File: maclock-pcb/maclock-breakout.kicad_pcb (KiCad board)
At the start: 2 copper layers, 70.5 x 26.5 mm, 24 parts, among them J1 53398-0271, J2 53398-0471, J3 53398-0271, J4 Pi GPIO, SW1 TSB001A3518A, SW2 TSB001A3518A, U1 PAM8302AASCR, U2 SN74LVC1G17DBVR, U3 TPS7A2030PDBVR

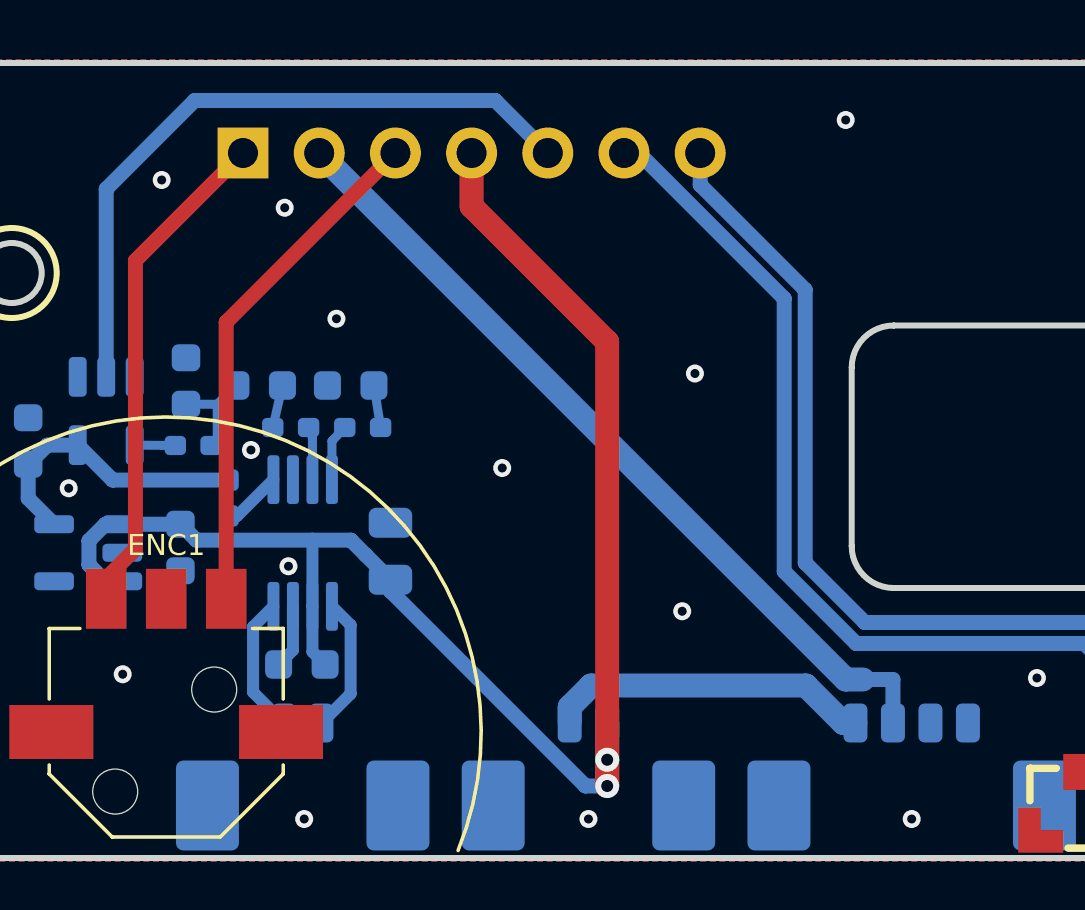
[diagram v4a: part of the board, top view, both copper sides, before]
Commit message: Breakout: spare C6 pads for a second amp input pole
R3/C1 is a single pole at 16 kHz, so it takes only about 24 dB off the
Pi's PWM noise near the PAM8302A's own 200-300 kHz switching frequency,
where a class-D amp can fold it back into the audio band. TI says as much
for DAC-fed class-D amps (TPA2011D1), and the Pi's own audio, which uses
the same buffer-on-LDO plus single RC as rev 2026.11, drives headphones,
not a switching amp.

C6 is a 470 pF C0G 0402 (Samsung CL05C471JB5NNNC, LCSC C307449) across
IN+ and IN-. With R4/R5 and the chip's internal 10 kOhm inputs it adds a
pole near 20 kHz: about 46 dB at 250 kHz instead of 24, for about 1 dB at
10 kHz. Rev 2026.10 had the same single pole and none of its measured
noise traced to this, so C6 is not fitted (DNP, off the BOM and the
placement file); solder it on only if a 2026.11 board hisses or whistles.

Layout: R5 and C6 stand vertically side by side east of R4, so C6's pads
sit on the IN+ run from R4 and the IN- run to U1 pin 4. C2, C3 and R4
stay below the Dial A / Dial B labels. NT1 turns vertical with its GND
pad on J2 pin 3, so the Pi's ground still joins the board ground at the
power connector. The schematic shows C6 as a small capacitor across the
IN+/IN- wires.

ERC 0. DRC 0 errors, 0 unconnected, schematic parity clean; only the
existing title-text thickness warning.
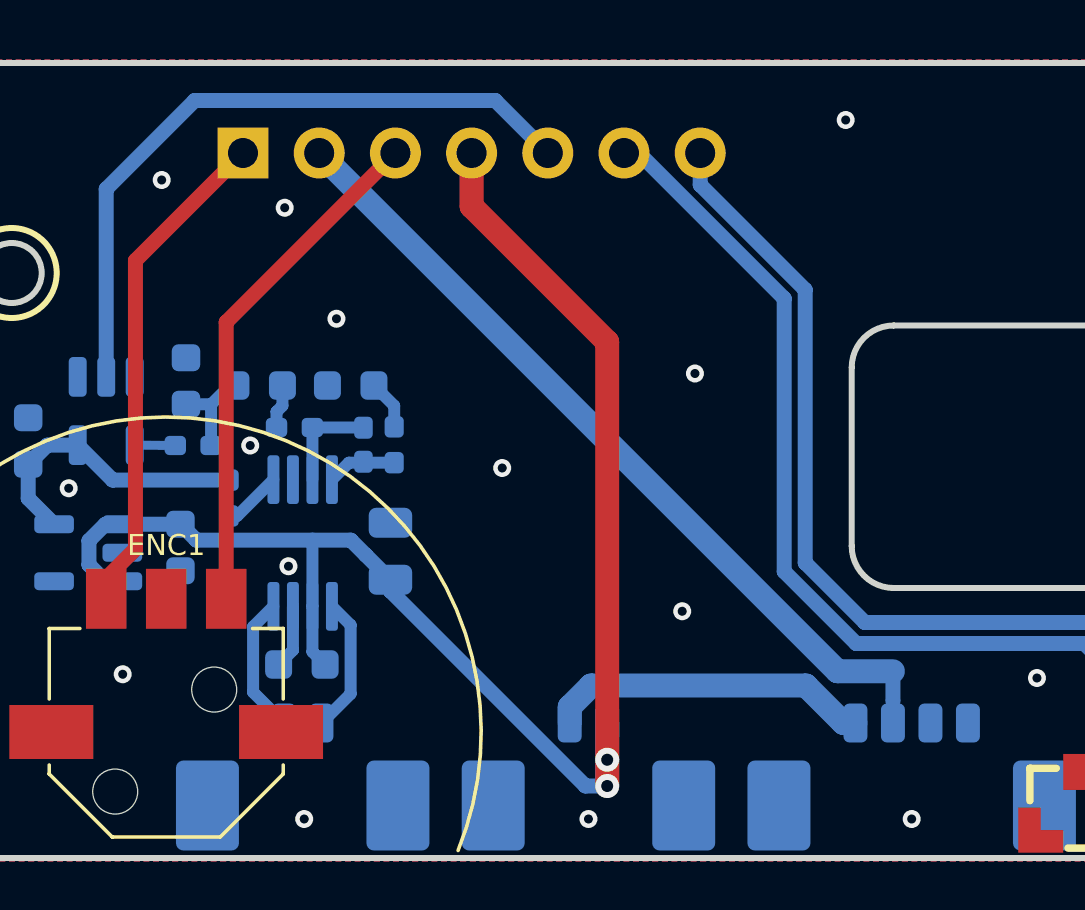
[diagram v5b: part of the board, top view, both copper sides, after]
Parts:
- added C6: 470pF, Capacitor_SMD:C_0402_1005Metric_Pad0.74x0.62mm_HandSolder, B.Cu at (133.5, 90.7)
- moved R5 1.20 mm to (134.5, 90.7), turned to -90 degrees
- moved NT1 0.55 mm to (151.1, 98.8), turned to -90 degrees
- moved R4 0.12 mm to (131.2, 90.2)
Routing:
- net Net-(U1-IN+): track 1.76 -> 3.44 mm
- net GND: track 3.59 -> 2.14 mm
- net /GND_PI: track 25.4 -> 26.3 mm

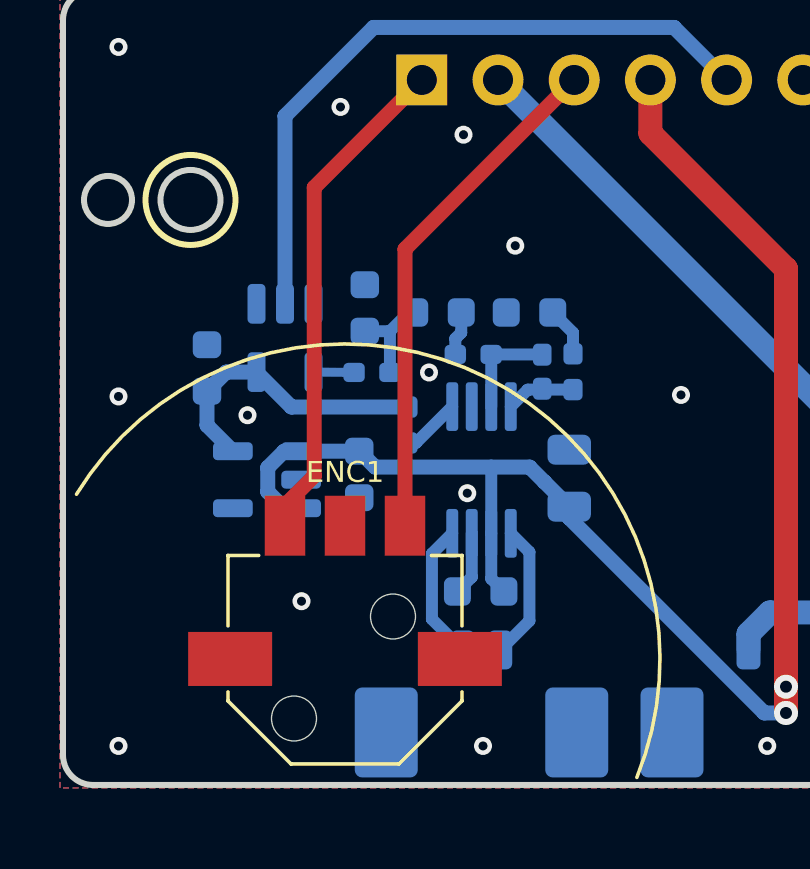
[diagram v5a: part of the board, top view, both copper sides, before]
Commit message: Breakout: ENC1 is a HUANO 4.5 laid flat, pins north, fitted by hand
No vertical encoder at LCSC, DigiKey or Mouser grips the dial: the bores
are too loose or too short. A HUANO 4.5 mm mouse-wheel encoder laid on its
back does: its 1.74 mm bore and 5 mm-thick body reach the full-width part of
the dial's tapered shaft. Nothing like it is sold where PCBway buys, so ENC1
is fitted by hand.

- maclock:RotaryEncoder_HUANO_4.5mm_LayFlat_SMD, origin on the bore at the
  old ENC1 spot, pins pointing north. Top-side pads at 2.5 mm pitch for the
  pins, bent down, plus two MP pads for the frame's clip legs. HUANO
  publishes no drawing, so the pads run 2.8 mm north from just outside the
  body (estimated from the listing photo) to catch the pins wherever they
  land. No paste, thermal reliefs on the GND pads, no 3D model. E8E8
  footprint and model removed.
- Pin order assumed C-B-A with the common at one end, as on HOAUC's and
  TT's mouse-wheel encoders: C (west pad) = GND, B = ENC_B, A = ENC_A.
  Turning the part face-down swaps the two ends.
- ENC_A and ENC_B re-routed on F.Cu to the new pads; nothing else moves.
- ENC1 is out of the BOM and placement files (not DNP: it is fitted, just
  not by PCBway). Symbol renamed maclock:RotaryEncoder_HUANO_4.5mm, with
  Amazon as the supplier; the schematic note and README say how to fit it.

DRC as before (one text-thickness warning), 0 unconnected, schematic parity
clean, ERC 0.
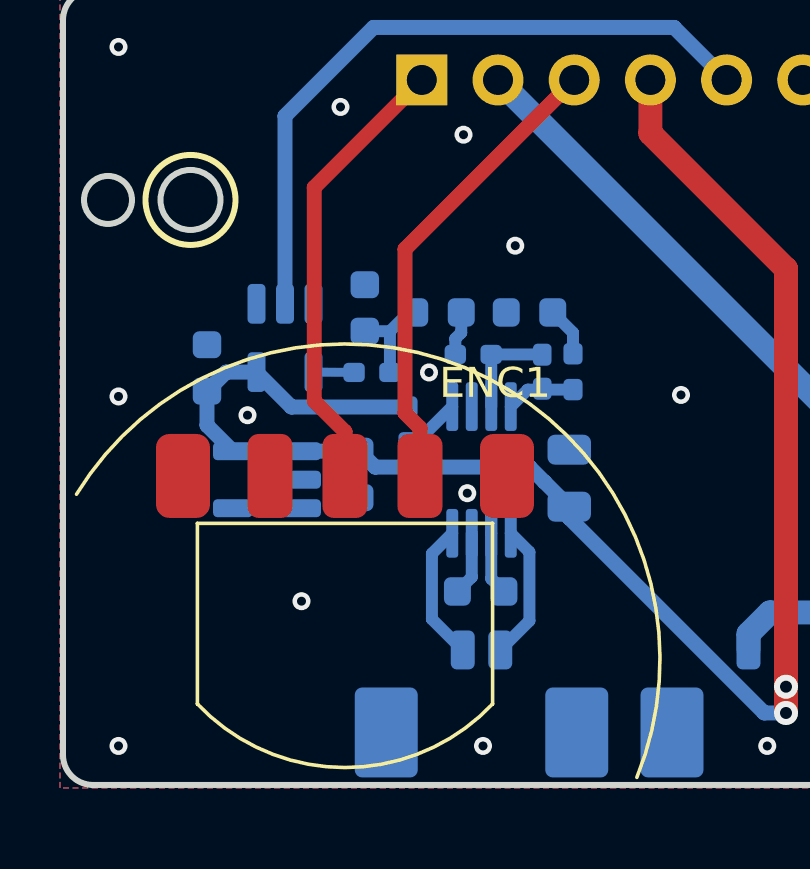
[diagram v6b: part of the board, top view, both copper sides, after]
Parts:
- ENC1: value E8E8-3.2C60-9B34 -> HUANO 4.5; footprint maclock:RotaryEncoder_E8E8-3.2C60-9B34_SMD -> maclock:RotaryEncoder_HUANO_4.5mm_LayFlat_SMD
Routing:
- net /ENC_B: track 16.7 -> 15.1 mm
- net /ENC_A: track 17.2 -> 15.7 mm
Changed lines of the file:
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@@
 		)
 	)
-	(footprint "maclock:RotaryEncoder_E8E8-3.2C60-9B34_SMD"
+	(footprint "maclock:RotaryEncoder_HUANO_4.5mm_LayFlat_SMD"
 		(layer "F.Cu")
 		(at 126.9 100.3)
-		(descr "F-Switch E8E8-3.2C60-9B34 SMD mouse-wheel encoder, 7.8 x 6.95 x 3.2 mm, 1.74 mm hex bore perpendicular to the board, 9 pulse / 18 detent (dicomon item 1037). Origin = bore centre. Copper is the proto board Dial land the encoder was soldered to; body outline measured from a real part. Silk carries the body outline and the 21 mm wheel circle, clipped to the maclock-breakout board edge.")
-		(tags "encoder wheel mouse F-Switch E8E8 hex bore")
+		(descr "HUANO 4.5 mm mouse-wheel encoder (sold as MECCANIXITY, Amazon B0C13ZZVT5) laid on its back with the 1.74 mm hex bore up, pins pointing north and bent down onto top-side pads; the MP pads take the frame's two clip legs, bent down the same way. Origin = bore centre. HUANO publishes no drawing: the 9.6 mm width and 2.5 mm pin pitch are the listing's, and the bore sits about 4.4 mm from the pin edge and 3.5 mm from the domed end (estimated from the listing photo), so the pads run 2.8 mm north to catch the bent pins wherever they land. Pin order assumed C-B-A with the common at one end, as on HOAUC's and TT's mouse-wheel encoders; turning the part face-down swaps the two ends. Hand-fitted, so no paste.")
+		(tags "encoder wheel mouse HUANO 4.5 hex bore lay flat")
 		(property "Reference" "ENC1"
-			(at 0 -6.225 0)
+			(at 5 -9.2 0)
 			(layer "F.SilkS")
 			(effects
 				(font
-					(size 0.7 0.7)
+					(size 1 1)
 					(thickness 0.15)
 				)
 			)
 		)
-		(property "Value" "E8E8-3.2C60-9B34"
-			(at 0 4.6 0)
+		(property "Value" "HUANO 4.5"
+			(at 0 2.4 0)
 			(layer "F.Fab")
 			(effects
@@
 			)
 		)
-		(property "Datasheet" "https://www.dicomon.com/index.php?ctl=Product&met=detail&item_id=1037"
+		(property "Datasheet" ""
 			(at 0 0 0)
 			(layer "F.Fab")
@@
 			)
 		)
-		(property "Description" "F-Switch E8E8-3.2C60-9B34 SMD mouse-wheel encoder, 9 pulse / 18 detent, 1.74 mm hex bore; MP = the cover's solder tabs"
+		(property "Description" "HUANO 4.5 mm mouse-wheel encoder laid on its back, 1.74 mm hex bore up, legs bent down onto top-side pads; MP = the frame's clip legs. Hand-fitted"
 			(at 0 0 0)
 			(layer "F.Fab")
@@
 			)
 		)
-		(property "Manufacturer" "F-Switch"
+		(property "Manufacturer" "HUANO"
 			(at 0 0 0)
 			(layer "F.Fab")
@@
 			)
 		)
-		(property "MPN" "E8E8-3.2C60-9B34"
+		(property "MPN" ""
 			(at 0 0 0)
 			(layer "F.Fab")
@@
 			)
 		)
-		(property "Supplier" "dicomon"
+		(property "Supplier" "Amazon"
 			(at 0 0 0)
 			(layer "F.Fab")
@@
 			)
 		)
-		(property "Supplier Link" "https://www.dicomon.com/index.php?ctl=Product&met=detail&item_id=1037"
+		(property "Supplier Link" "https://www.amazon.com/dp/B0C13ZZVT5"
 			(at 0 0 0)
 			(layer "F.Fab")
@@
 			)
 		)
-		(attr smd)
+		(zone_connect 1)
+		(attr smd exclude_from_pos_files exclude_from_bom)
 		(duplicate_pad_numbers_are_jumpers no)
 		(fp_line
-			(start -3.9 -3.45)
-			(end -3.9 -1.1)
+			(start -4.92 -4.52)
+			(end 4.92 -4.52)
 			(stroke
 				(width 0.12)
@@
 		)
 		(fp_line
-			(start -3.9 -3.45)
-			(end -2.875 -3.45)
+			(start -4.92 1.5)
+			(end -4.92 -4.52)
 			(stroke
 				(width 0.12)
@@
 		)
 		(fp_line
-			(start -3.9 1.1)
-			(end -3.9 1.4)
+			(start 4.92 -4.52)
+			(end 4.92 1.5)
 			(stroke
 				(width 0.12)
@@
 			(layer "F.SilkS")
 		)
-		(fp_line
-			(start -3.9 1.4)
-			(end -1.8 3.5)
+		(fp_arc
+			(start -8.95 -5.4907)
+			(mid 4.7364 -9.3711)
+			(end 9.7287 3.95)
 			(stroke
 				(width 0.12)
@@
 			(layer "F.SilkS")
 		)
-		(fp_line
-			(start -1.8 3.5)
-			(end 1.8 3.5)
+		(fp_arc
+			(start 4.92 1.5)
+			(mid 0 3.62)
+			(end -4.92 1.5)
 			(stroke
 				(width 0.12)
@@
 			(layer "F.SilkS")
 		)
-		(fp_line
-			(start 2.875 -3.45)
-			(end 3.9 -3.45)
+		(fp_rect
+			(start -6.55 -7.85)
+			(end 6.55 3.9)
 			(stroke
-				(width 0.12)
+				(width 0.05)
 				(type default)
 			)
-			(layer "F.SilkS")
+			(fill no)
+			(layer "F.CrtYd")
 		)
 		(fp_line
-			(start 3.9 -3.45)
-			(end 3.9 -1.1)
+			(start -5.5 -5.6)
+			(end -5.1 -7.9)
 			(stroke
-				(width 0.12)
+				(width 0.1)
 				(type default)
 			)
-			(layer "F.SilkS")
+			(layer "F.Fab")
 		)
 		(fp_line
-			(start 3.9 1.1)
-			(end 3.9 1.4)
+			(start -4.8 -4.4)
+			(end 4.8 -4.4)
 			(stroke
-				(width 0.12)
+				(width 0.1)
 				(type default)
 			)
-			(layer "F.SilkS")
+			(layer "F.Fab")
 		)
 		(fp_line
-			(start 3.9 1.4)
-			(end 1.8 3.5)
+			(start -4.8 -3.6)
+			(end -5.5 -5.6)
 			(stroke
-				(width 0.12)
+				(width 0.1)
 				(type default)
 			)
-			(layer "F.SilkS")
+			(layer "F.Fab")
 		)
-		(fp_arc
-			(start -8.95 -5.4907)
-			(mid 4.7364 -9.3711)
-			(end 9.7287 3.95)
+		(fp_line
+			(start -4.8 1.5)
+			(end -4.8 -4.4)
 			(stroke
-				(width 0.12)
+				(width 0.1)
 				(type default)
 			)
-			(layer "F.SilkS")
+			(layer "F.Fab")
 		)
-		(fp_rect
-			(start -5.5 -5.7)
-			(end 5.5 3.75)
+		(fp_line
+			(start 4.8 -4.4)
+			(end 4.8 1.5)
 			(stroke
-				(width 0.05)
+				(width 0.1)
 				(type default)
 			)
-			(fill no)
-			(layer "F.CrtYd")
+			(layer "F.Fab")
 		)
 		(fp_line
-			(start -3.9 -3.45)
-			(end 3.9 -3.45)
+			(start 4.8 -3.6)
+			(end 5.5 -5.6)
 			(stroke
 				(width 0.1)
@@
 		)
 		(fp_line
-			(start -3.9 1.4)
-			(end -3.9 -3.45)
+			(start 5.5 -5.6)
+			(end 5.1 -7.9)
 			(stroke
 				(width 0.1)
@@
 			(layer "F.Fab")
 		)
-		(fp_line
-			(start -1.8 3.5)
-			(end -3.9 1.4)
+		(fp_rect
+			(start -2.9 -6.9)
+			(end -2.1 -4.4)
 			(stroke
 				(width 0.1)
 				(type default)
 			)
+			(fill no)
 			(layer "F.Fab")
 		)
-		(fp_line
-			(start 1.8 3.5)
-			(end -1.8 3.5)
+		(fp_rect
+			(start -0.4 -6.9)
+			(end 0.4 -4.4)
 			(stroke
 				(width 0.1)
 				(type default)
 			)
+			(fill no)
 			(layer "F.Fab")
 		)
-		(fp_line
-			(start 3.9 -3.45)
-			(end 3.9 1.4)
+		(fp_rect
+			(start 2.1 -6.9)
+			(end 2.9 -4.4)
 			(stroke
 				(width 0.1)
 				(type default)
 			)
+			(fill no)
 			(layer "F.Fab")
 		)
-		(fp_line
-			(start 3.9 1.4)
-			(end 1.8 3.5)
+		(fp_arc
+			(start 4.8 1.5)
+			(mid 0 3.5)
+			(end -4.8 1.5)
 			(stroke
 				(width 0.1)
@@
 		(fp_circle
 			(center 0 0)
-			(end 1.85 0)
+			(end 1.9 0)
 			(stroke
 				(width 0.1)
@@
 		)
 		(fp_text user "${REFERENCE}"
-			(at 0 -2.4 0)
+			(at 0 1.2 0)
 			(layer "F.Fab")
 			(effects
@@
 			)
 		)
-		(pad "" np_thru_hole circle
-			(at -1.7 1.985)
-			(size 1.5 1.5)
-			(drill 1.5)
-			(layers "*.Cu" "*.Mask")
-		)
-		(pad "" np_thru_hole circle
-			(at 1.6 -1.415)
-			(size 1.5 1.5)
-			(drill 1.5)
-			(layers "*.Cu" "*.Mask")
-		)
-		(pad "A" smd rect
-			(at 2 -4.44)
-			(size 1.35 2)
-			(layers "F.Cu" "F.Mask" "F.Paste")
+		(pad "A" smd roundrect
+			(at 2.5 -6.1)
+			(size 1.5 2.8)
+			(layers "F.Cu" "F.Mask")
+			(roundrect_rratio 0.25)
 			(net "/ENC_A")
-			(thermal_bridge_angle 45)
 		)
-		(pad "B" smd rect
-			(at -2 -4.44)
-			(size 1.35 2)
-			(layers "F.Cu" "F.Mask" "F.Paste")
+		(pad "B" smd roundrect
+			(at 0 -6.1)
+			(size 1.5 2.8)
+			(layers "F.Cu" "F.Mask")
+			(roundrect_rratio 0.25)
 			(net "/ENC_B")
-			(thermal_bridge_angle 45)
 		)
-		(pad "C" smd rect
-			(at 0 -4.44)
-			(size 1.35 2)
-			(layers "F.Cu" "F.Mask" "F.Paste")
+		(pad "C" smd roundrect
+			(at -2.5 -6.1)
+			(size 1.5 2.8)
+			(layers "F.Cu" "F.Mask")
+			(roundrect_rratio 0.25)
 			(net "GND")
-			(thermal_bridge_angle 45)
 		)
-		(pad "MP" smd rect
-			(at -3.83 0)
-			(size 2.8 1.8)
-			(layers "F.Cu" "F.Mask" "F.Paste")
+		(pad "MP" smd roundrect
+			(at -5.4 -6.1)
+			(size 1.8 2.8)
+			(layers "F.Cu" "F.Mask")
+			(roundrect_rratio 0.25)
 			(net "GND")
-			(thermal_bridge_angle 45)
 		)
-		(pad "MP" smd rect
-			(at 3.83 0)
-			(size 2.8 1.8)
-			(layers "F.Cu" "F.Mask" "F.Paste")
+		(pad "MP" smd roundrect
+			(at 5.4 -6.1)
+			(size 1.8 2.8)
+			(layers "F.Cu" "F.Mask")
+			(roundrect_rratio 0.25)
 			(net "GND")
-			(thermal_bridge_angle 45)
 		)
 		(embedded_fonts no)
-		(model "${KIPRJMOD}/maclock.3dshapes/E8E8-3.2C60-9B34.step"
-			(offset
-				(xyz 0 0 0)
-			)
-			(scale
-				(xyz 1 1 1)
-			)
-			(rotate
-				(xyz 0 0 0)
-			)
-		)
 	)
 	(footprint "lcsc:SW-SMD_TSB001XXXX"
@@
 	)
 	(segment
+		(start 128.9 92.1)
+		(end 129.4 92.6)
+		(width 0.5)
+		(layer "F.Cu")
+		(net "/ENC_A")
+	)
+	(segment
+		(start 129.4 92.6)
+		(end 129.4 94.2)
+		(width 0.5)
+		(layer "F.Cu")
+		(net "/ENC_A")
+	)
+	(segment
 		(start 128.9 86.64)
-		(end 128.9 95.86)
+		(end 128.9 92.1)
 		(width 0.5)
 		(layer "F.Cu")
@@
 	)
 	(segment
-		(start 124.9 95.175)
-		(end 124.9 95.86)
+		(start 125.875 91.7)
+		(end 126.9 92.725)
 		(width 0.5)
 		(layer "F.Cu")
@@
 	)
 	(segment
-		(start 129.46 81)
-		(end 125.875 84.585)
+		(start 126.9 92.725)
+		(end 126.9 94.2)
 		(width 0.5)
 		(layer "F.Cu")
@@
 	)
 	(segment
-		(start 125.875 84.585)
-		(end 125.875 94.2)
+		(start 129.46 81)
+		(end 125.875 84.585)
 		(width 0.5)
 		(layer "F.Cu")
@@
 	)
 	(segment
-		(start 125.875 94.2)
-		(end 124.9 95.175)
+		(start 125.875 84.585)
+		(end 125.875 91.7)
 		(width 0.5)
 		(layer "F.Cu")
